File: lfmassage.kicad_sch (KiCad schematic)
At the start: 1 part, among them IC1 EFM8BB31F16G-D-QFN24

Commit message: 2022-07-11
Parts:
- removed IC1: EFM8BB31F16G-D-QFN24, EFM8BB31F16G-D-QFN24:EFM8BB31F16GDQFN24, symbol EFM8BB31F16G-D-QFN24:EFM8BB31F16G-D-QFN24
- added B1: MLT-5030, MLT-5030:MLT-5030, symbol MLT-5030:MLT-5030
- added C1, C10, C11, C12, C2: 100nF, Capacitor_SMD:C_0402_1005Metric, symbol Device:C
- added C3, C4, C8: 10uF, Capacitor_SMD:C_0603_1608Metric, symbol Device:C
- added C5, C7: 1uF, Capacitor_SMD:C_0402_1005Metric, symbol Device:C
- added C6: 10nF, Capacitor_SMD:C_0402_1005Metric, symbol Device:C
- added C9: 10uF, Capacitor_SMD:C_1206_3216Metric, symbol Device:C
- added D1: MHS110KECT, MHS110KECT:LED-ARRAY-SMD_3P-L3.00-W1.50-R-RD, symbol MHS110KECT:MHS110KECT
- added D10: IR LED, XL-1608UWC-04:LED0805-RD, symbol XL-2012HIRC-850:XL-2012HIRC-850
- added D11, D9: RED LED, XL-1608UWC-04:LED0805-RD, symbol XL-2012HIRC-850:XL-2012HIRC-850
- added D2, D3, D4: 1N4148W-7-F, 1N4148W-7-F:SOD-123_L2.7-W1.6-LS3.7-RD-1, symbol 1N4148W-7-F:1N4148W-7-F
- added D5: DSK34, Diode_SMD:D_SOD-123, symbol Device:D
- added D6, D7, D8: LED, XL-1608UWC-04:XL-1608UWC-04, symbol XL-1608UWC-04:XL-1608UWC-04
- added E1: SparkGap, Electrode:Electrode, symbol Device:SparkGap
- added IC1: STM32L010F4P6, STM32L010F4P6:SOP65P640X120-20N, symbol STM32L010F4P6:STM32L010F4P6
- added J1: USB4125-GF-A-0190, USB4125-GF-A-0190:USB4125GFA0190, symbol USB4125-GF-A-0190:USB4125-GF-A-0190
- added J2: SWD, Connector_PinHeader_2.54mm:PinHeader_1x05_P2.54mm_Vertical, symbol Connector_Generic:Conn_01x05
- added J3: 53261-0271, Connector_Molex:Molex_PicoBlade_53261-0271_1x02-1MP_P1.25mm_Horizontal, symbol Connector_Generic_MountingPin:Conn_01x02_MountingPin
- added L1: 4.7uH, Inductor_SMD:L_Bourns-SRN4018, symbol CD43YP0403-330M:CD43YP0403-330M
- added M1, M2, M3, M4, M5, M6, M7, M8: MountingHole, MountingHole:MountingHole_2.2mm_M2, symbol Mechanical:MountingHole
- added Q1, Q2, Q3, Q4, Q5, Q6: N-FET, Package_TO_SOT_SMD:SOT-23, symbol Device:Q_NMOS_GSD
- added R1, R2, R5: 47k, Resistor_SMD:R_0402_1005Metric, symbol Device:R
- added R10, R8, R9: 100, Resistor_SMD:R_0402_1005Metric, symbol Device:R
- added R3: 10k, Resistor_SMD:R_0402_1005Metric, symbol Device:R
- added R4: 680, Resistor_SMD:R_0402_1005Metric, symbol Device:R
- added R6: 180k, Resistor_SMD:R_0402_1005Metric, symbol Device:R
- added R7: 8.2k, Resistor_SMD:R_0402_1005Metric, symbol Device:R
- added SW1, SW2, SW3: TS24CA, TS24CA:TS24CA, symbol TS24CA:TS24CA
- added U1: MCP73831-2-OT, Package_TO_SOT_SMD:SOT-23-5, symbol Battery_Management:MCP73831-2-OT
- added U2: MT3540, Package_TO_SOT_SMD:SOT-23-5, symbol Regulator_Switching:MT3608
- added U3: RS3236-2_8YF5, RS3236-2.8YF5:SOT-23-5_L2.9-W1.6-P0.95-LS2.8-BL, symbol RS3236-2.8YF5:RS3236-2_8YF5
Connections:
- new net: D5.2 (A), L1.2, U2.1 (SW)
- new net: R6.1, R7.2, U2.3 (FB)
- new net: C8.1, D3.1 (C), L1.1, U2.5 (IN)
- new net: D2.2 (A), J1.A9 (VBUS_1), J1.B9 (VBUS_2)
- new net: D11.2 (A), R10.1
- new net: D10.2 (A), R9.1
- new net: C6.2, U3.4 (BP)
- new net: D9.2 (A), R8.1
- new net: B1.3 (-), D4.2 (A), Q1.3 (D)
- new net: D1.4 (-), R4.2
- new net: R3.2, U1.5 (PROG)
- new net: D10.1 (K), D11.1 (K), D9.1 (K), Q6.3 (D)
- new net: E1.1, Q2.2 (S), Q3.3 (D)
- new net: E1.2, Q4.2 (S), Q5.3 (D)
- new net: IC1.1 (PB9-BOOT0), R2.2
- new net: R4.1, U1.1 (STAT)
- new net +2V8: B1.2 (+), C2.1, C3.1, C7.1, D4.1 (C), IC1.16 (VDD), IC1.5 (VDDA), J2.1 (Pin_1), R1.1, R10.2, R8.2, R9.2, SW1.4, SW2.4, SW3.4, U3.5 (OUT)
- new net BATT: C4.1, C5.2, D3.2 (A), J3.1 (Pin_1), U1.3 (VBAT), U3.1 (IN), U3.3 (EN)
- new net GND: B1.1 (NC), C1.1, C10.2, C11.2, C12.2, C2.2, C3.2, C4.2, C5.1, C6.1, C7.2, C8.2, C9.2, D6.1 (K), D7.1 (K), D8.1 (K), IC1.15 (VSS), J1.A12 (GND_1), J1.B12 (GND_2), J1.MH1, J1.MH2, J1.MH3, J1.MH4, J2.3 (Pin_3), J3.2 (Pin_2), J3.MP (MountPin), Q1.2 (S), Q3.2 (S), Q5.2 (S), Q6.2 (S), R2.1, R3.1, R5.2, R7.1, SW1.1, SW1.2, SW2.1, SW2.2, SW3.1, SW3.2, U1.2 (VSS), U2.2 (GND), U3.2 (GND)
- new net HV: C9.1, D5.1 (K), Q2.3 (D), Q4.3 (D), R6.2
- new net PA0: IC1.6 (PA0-CK_IN), Q6.1 (G)
- new net PA1: IC1.7 (PA1), R5.1, U2.4 (EN)
- new net PA10: IC1.18 (PA10), Q1.1 (G)
- new net PA2: IC1.8 (PA2), Q2.1 (G), Q5.1 (G)
- new net PA3: IC1.9 (PA3), Q3.1 (G), Q4.1 (G)
- new net PA4: C10.1, IC1.10 (PA4), SW1.3
- new net PA5: C11.1, IC1.11 (PA5), SW2.3
- new net PA6: C12.1, IC1.12 (PA6), SW3.3
- new net PA7: D6.2 (A), IC1.13 (PA7)
- new net PA9: D8.2 (A), IC1.17 (PA9)
- new net PB1: D7.2 (A), IC1.14 (PB1)
- new net SWCLK: IC1.20 (PA14), J2.2 (Pin_2)
- new net SWDIO: IC1.19 (PA13), J2.4 (Pin_4)
- new net VBUS: D1.1 (+), D2.1 (C), U1.4 (VDD)
- new net nRST: C1.2, IC1.4 (NRST), J2.5 (Pin_5), R1.2
- no-connect marks 0 -> 3
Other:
- note added: "4kHz 50%"

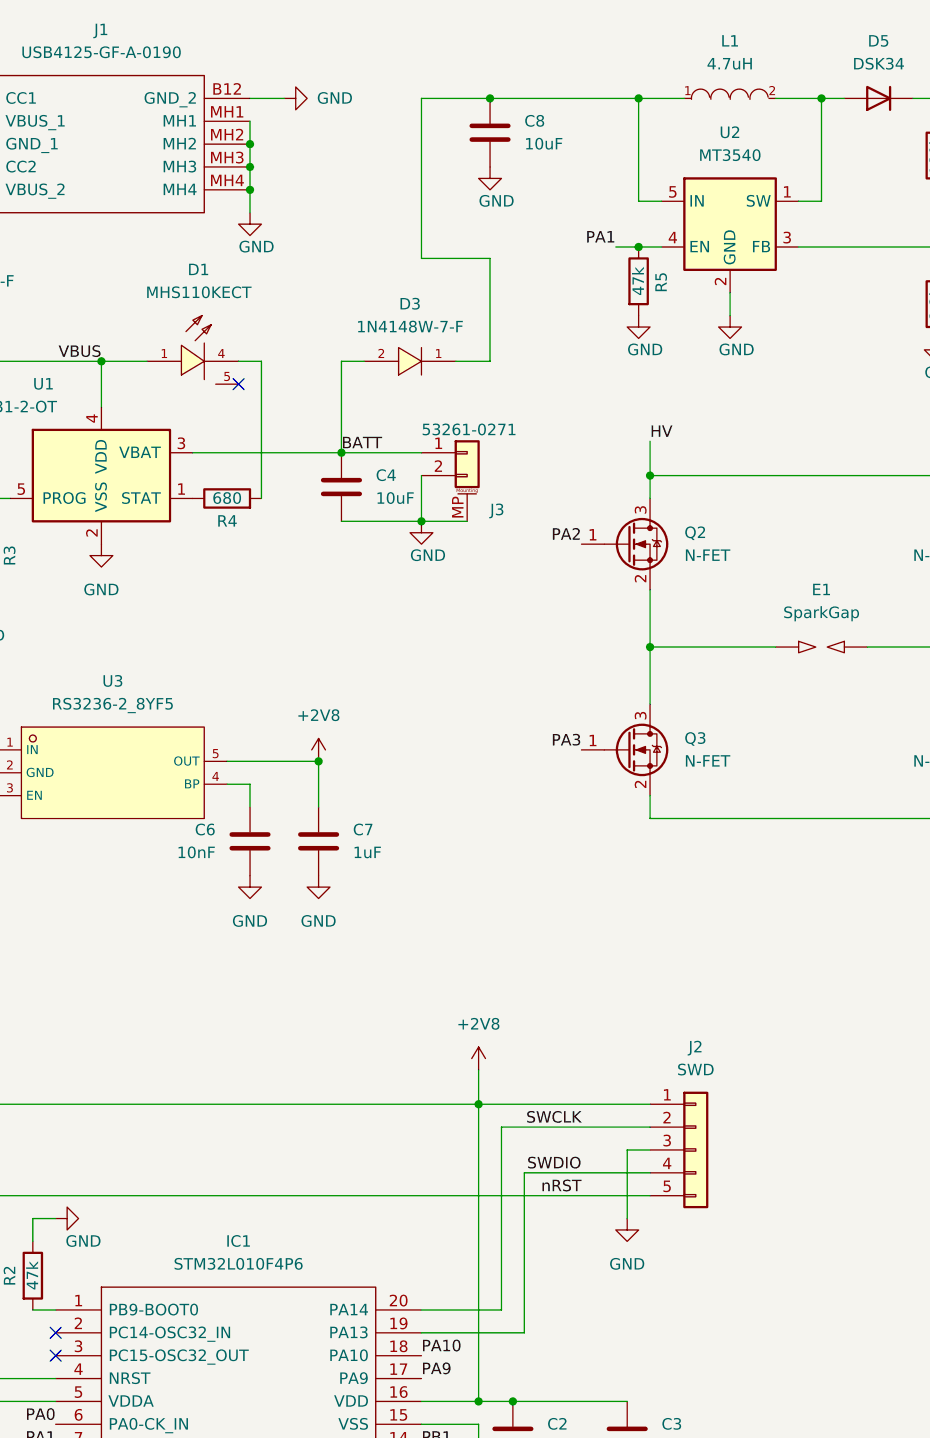
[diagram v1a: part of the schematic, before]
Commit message: MCU change to STM32L031F6P6
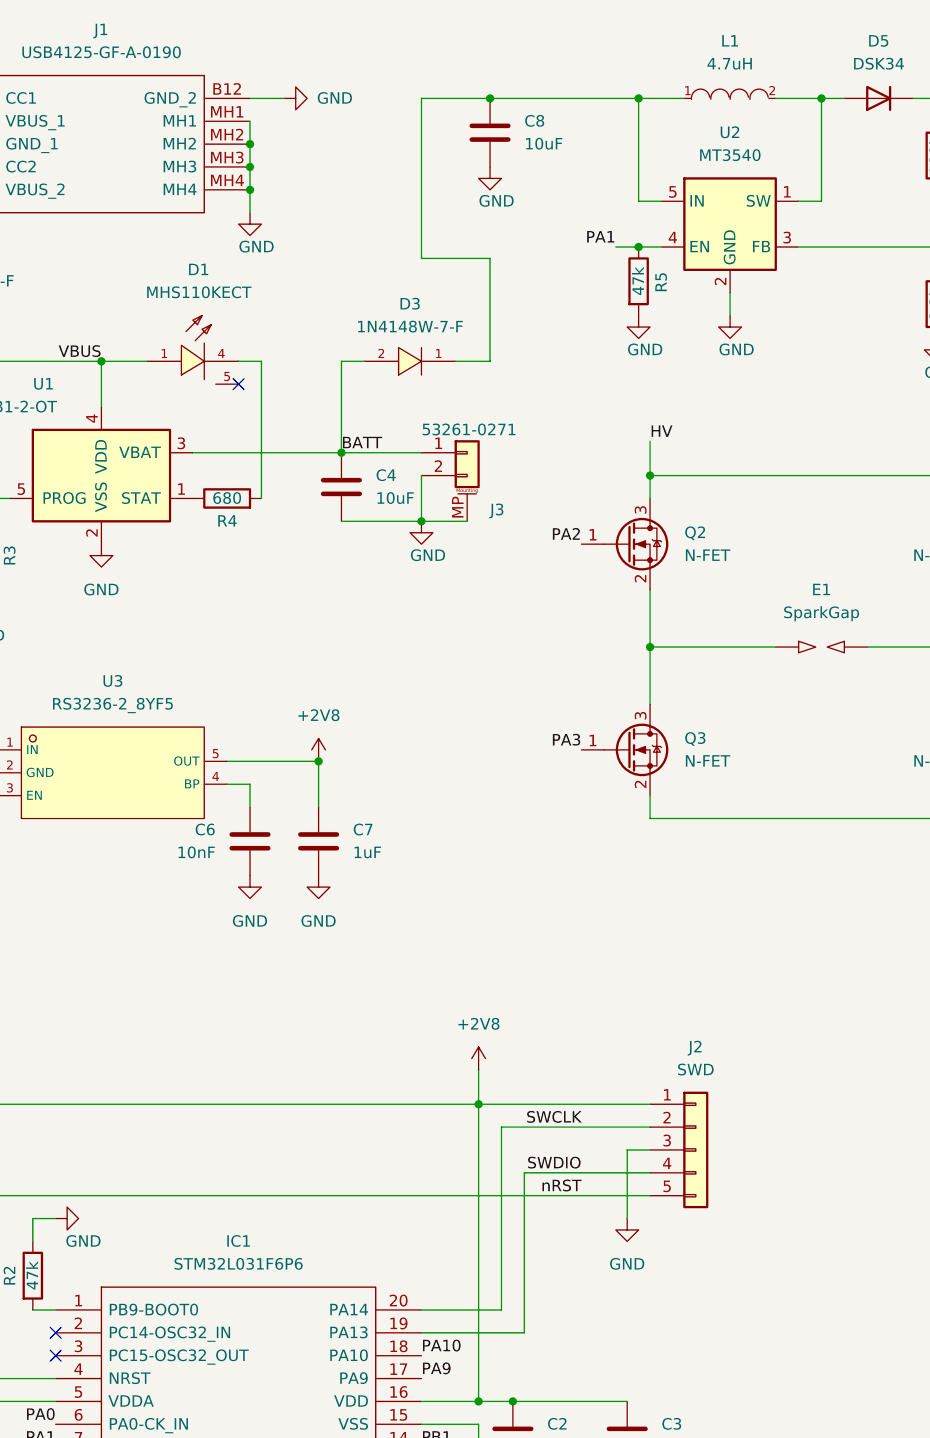
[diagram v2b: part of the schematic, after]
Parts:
- IC1: value STM32L010F4P6 -> STM32L031F6P6; LCSC Part C529415 -> C115208; MPN STM32L010F4P6 -> STM32L031F6P6
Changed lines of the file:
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@@
     (in_bom yes) (on_board yes) (fields_autoplaced)
     (property "Reference" "IC1" (id 0) (at 64.77 154.94 0))
-    (property "Value" "STM32L010F4P6" (id 1) (at 64.77 157.48 0))
+    (property "Value" "STM32L031F6P6" (id 1) (at 64.77 157.48 0))
     (property "Footprint" "STM32L010F4P6:SOP65P640X120-20N" (id 2) (at 81.28 160.02 0)
       (effects (font (size 1.27 1.27)) (justify left) hide)
     )
-    (property "Datasheet" "https://www.st.com/resource/en/datasheet/stm32l010f4.pdf" (id 3) (at 81.28 162.56 0)
-      (effects (font (size 1.27 1.27)) (justify left) hide)
-    )
-    (property "MPN" "STM32L010F4P6" (id 9) (at 81.28 177.8 0)
-      (effects (font (size 1.27 1.27)) (justify left) hide)
-    )
-    (property "LCSC Part" "C529415" (id 5) (at 44.45 162.56 0)
+    (property "Datasheet" "https://datasheet.lcsc.com/lcsc/1809242106_STMicroelectronics-STM32L031F6P6_C115208.pdf" (id 3) (at 81.28 162.56 0)
+      (effects (font (size 1.27 1.27)) (justify left) hide)
+    )
+    (property "MPN" "STM32L031F6P6" (id 9) (at 81.28 177.8 0)
+      (effects (font (size 1.27 1.27)) (justify left) hide)
+    )
+    (property "LCSC Part" "C115208" (id 5) (at 44.45 162.56 0)
       (effects (font (size 1.27 1.27)) hide)
     )
@@
     )
     (path "/71a3f1b0-2f2f-457c-93f6-3270b0e90e33"
-      (reference "IC1") (unit 1) (value "STM32L010F4P6") (footprint "STM32L010F4P6:SOP65P640X120-20N")
+      (reference "IC1") (unit 1) (value "STM32L031F6P6") (footprint "STM32L010F4P6:SOP65P640X120-20N")
     )
     (path "/accd74b8-d7b4-4c27-8505-bb1ff747fb4f"
